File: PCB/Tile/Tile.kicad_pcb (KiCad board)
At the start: 2 copper layers, 100 x 86.6 mm, 41 parts, among them J1 Conn_01x05_Male, U1 HT16K33-28SOP

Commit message: [update] Tileの配線改善(DRC, 名前, ロゴ) #3
* DRCエラー(D17-Pad1)を修正
* 5-PINヘッダの名前をJ1からCN1に修正
* GardeningBoardのロゴの"Gardening"文字を右に移動
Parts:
- removed J1: Conn_01x05_Male, Connector_PinHeader_2.54mm:PinHeader_1x05_P2.54mm_Vertical
- added CN1: Conn_01x05_Male, Connector_PinHeader_2.54mm:PinHeader_1x05_P2.54mm_Vertical, F.Cu at (125.0, 92.5)
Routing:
- net Net-(D21-Pad2): track 61.7 -> 60.7 mm
- net GND: vias 47 -> 46

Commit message: (Tile) スレーブアドレス選択のシルク誤りを修正 #17
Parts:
- removed G***: LOGO, logos:logo_750dpi
- removed JP3: A0, Jumper:SolderJumper-2_P1.3mm_Open_RoundedPad1.0x1.5mm
- added A0: A0, Jumper:SolderJumper-2_P1.3mm_Open_RoundedPad1.0x1.5mm, B.Cu at (122.1, 79.3)
- renumbered JP2 to A1, JP1 to A2
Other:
- board text added: "@ext_sui 2020.09"
- board text added: "Tile Growing v1.1"
- board text removed: "@ext_sui 2020.05"
- board text removed: "Tile Growing v1.0"

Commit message: (Tile) ダイオードのシルクを D26 から D25 に修正 #17
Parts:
- renumbered D26 to D25
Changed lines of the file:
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@@
   (net 28 "Net-(D16-Pad2)")
   (net 29 "Net-(D17-Pad1)")
-  (net 30 "Net-(D26-Pad1)")
-  (net 31 +5V)
-  (net 32 "Net-(D9-Pad2)")
-  (net 33 "Net-(CN1-Pad4)")
+  (net 30 +5V)
+  (net 31 "Net-(D9-Pad2)")
+  (net 32 "Net-(CN1-Pad4)")
+  (net 33 "Net-(D25-Pad1)")
   (net_class Default "これはデフォルトのネット クラスです。"
     (clearance 0.2)
@@
     (add_net "Net-(D23-Pad2)")
     (add_net "Net-(D24-Pad2)")
-    (add_net "Net-(D26-Pad1)")
+    (add_net "Net-(D25-Pad1)")
     (add_net "Net-(D9-Pad2)")
     (add_net "Net-(JP1-Pad1)")
@@
       (net 4 "Net-(D10-Pad2)"))
     (pad 17 smd rect (at 4.7 -5.715 270) (size 2 0.6) (layers B.Cu B.Paste B.Mask)
-      (net 32 "Net-(D9-Pad2)"))
+      (net 31 "Net-(D9-Pad2)"))
     (pad 18 smd rect (at 4.7 -4.445 270) (size 2 0.6) (layers B.Cu B.Paste B.Mask)
       (net 27 "Net-(D24-Pad2)"))
@@
       (net 10 SDA))
     (pad 28 smd rect (at 4.7 8.255 270) (size 2 0.6) (layers B.Cu B.Paste B.Mask)
-      (net 31 +5V))
+      (net 30 +5V))
     (model ${KISYS3DMOD}/Package_SO.3dshapes/SOIC-28W_7.5x18.7mm_P1.27mm.wrl
       (at (xyz 0 0 0))
@@
     (fp_line (start 1.45 -0.7) (end -1.46 -0.7) (layer B.CrtYd) (width 0.05))
     (pad 1 smd rect (at -0.8 0 180) (size 0.8 0.8) (layers B.Cu B.Paste B.Mask)
-      (net 31 +5V))
+      (net 30 +5V))
     (pad 2 smd rect (at 0.8 0 180) (size 0.8 0.8) (layers B.Cu B.Paste B.Mask)
       (net 1 GND))
@@
     (tags "resistor 0603")
     (attr smd)
-    (fp_text reference D26 (at 3 0 180) (layer B.SilkS)
+    (fp_text reference D25 (at 3 0 180) (layer B.SilkS)
       (effects (font (size 1 1) (thickness 0.15)) (justify mirror))
     )
@@
     (fp_line (start -0.25 0) (end 0.25 -0.25) (layer B.SilkS) (width 0.15))
     (pad 1 smd rect (at -0.8 0 180) (size 0.8 0.8) (layers B.Cu B.Paste B.Mask)
-      (net 30 "Net-(D26-Pad1)"))
+      (net 33 "Net-(D25-Pad1)"))
     (pad 2 smd rect (at 0.8 0 180) (size 0.8 0.8) (layers B.Cu B.Paste B.Mask)
       (net 2 "Net-(D1-Pad1)"))
@@
     (fp_line (start -1.45 0.7) (end -1.45 -0.7) (layer B.SilkS) (width 0.12))
     (pad 2 smd rect (at 0.8 0 180) (size 0.8 0.8) (layers B.Cu B.Paste B.Mask)
-      (net 30 "Net-(D26-Pad1)"))
+      (net 33 "Net-(D25-Pad1)"))
     (pad 1 smd rect (at -0.8 0 180) (size 0.8 0.8) (layers B.Cu B.Paste B.Mask)
       (net 6 "Net-(JP1-Pad1)"))
@@
     (fp_line (start -1.45 0.7) (end -1.45 -0.7) (layer B.SilkS) (width 0.12))
     (pad 2 smd rect (at 0.8 0 180) (size 0.8 0.8) (layers B.Cu B.Paste B.Mask)
-      (net 30 "Net-(D26-Pad1)"))
+      (net 33 "Net-(D25-Pad1)"))
     (pad 1 smd rect (at -0.8 0 180) (size 0.8 0.8) (layers B.Cu B.Paste B.Mask)
       (net 7 "Net-(JP2-Pad1)"))
@@
       (net 8 "Net-(JP3-Pad1)"))
     (pad 2 smd rect (at 0.8 0 180) (size 0.8 0.8) (layers B.Cu B.Paste B.Mask)
-      (net 30 "Net-(D26-Pad1)"))
+      (net 33 "Net-(D25-Pad1)"))
     (model ${KISYS3DMOD}/Resistors_SMD.3dshapes/R_0603.wrl
       (at (xyz 0 0 0))
@@
     (fp_line (start -1.45 -0.7) (end -1.45 0.7) (layer F.SilkS) (width 0.12))
     (pad 2 smd rect (at 0.8 0 300) (size 0.8 0.8) (layers F.Cu F.Paste F.Mask)
-      (net 32 "Net-(D9-Pad2)"))
+      (net 31 "Net-(D9-Pad2)"))
     (pad 1 smd rect (at -0.8 0 300) (size 0.8 0.8) (layers F.Cu F.Paste F.Mask)
       (net 2 "Net-(D1-Pad1)"))
@@
     )
     (pad 1 thru_hole rect (at 0 0 90) (size 1.7 1.7) (drill 1) (layers *.Cu *.Mask)
-      (net 31 +5V))
+      (net 30 +5V))
     (pad 2 thru_hole oval (at 0 2.54 90) (size 1.7 1.7) (drill 1) (layers *.Cu *.Mask)
       (net 10 SDA))
@@
       (net 9 SCL))
     (pad 4 thru_hole oval (at 0 7.62 90) (size 1.7 1.7) (drill 1) (layers *.Cu *.Mask)
-      (net 33 "Net-(CN1-Pad4)"))
+      (net 32 "Net-(CN1-Pad4)"))
     (pad 5 thru_hole oval (at 0 10.16 90) (size 1.7 1.7) (drill 1) (layers *.Cu *.Mask)
       (net 1 GND))
@@
   (segment (start 129 139) (end 136 139) (width 0.25) (layer B.Cu) (net 29))
   (segment (start 136 139) (end 138 141) (width 0.25) (layer B.Cu) (net 29))
-  (segment (start 111.24713 81.753186) (end 111.24013 81.746186) (width 0.25) (layer B.Cu) (net 30))
-  (segment (start 115.03013 81.753186) (end 111.24713 81.753186) (width 0.25) (layer B.Cu) (net 30))
-  (segment (start 115.03013 80.253186) (end 115.03013 83.253186) (width 0.25) (layer B.Cu) (net 30))
-  (segment (start 128.695 86.75) (end 128.745 86.7) (width 0.5) (layer B.Cu) (net 31))
-  (segment (start 122.9 86.75) (end 128.695 86.75) (width 0.5) (layer B.Cu) (net 31))
-  (segment (start 128.745 88.755) (end 128.745 88.255) (width 0.5) (layer B.Cu) (net 31))
-  (segment (start 125 92.5) (end 128.745 88.755) (width 0.5) (layer B.Cu) (net 31))
-  (segment (start 128.745 88.255) (end 128.745 86.7) (width 0.5) (layer B.Cu) (net 31))
-  (segment (start 158.7 84.728718) (end 159.35 85.85) (width 0.25) (layer F.Cu) (net 32))
-  (via (at 159.35 85.85) (size 0.8) (drill 0.4) (layers F.Cu B.Cu) (net 32))
-  (segment (start 142.715 88.785) (end 142.715 86.7) (width 0.25) (layer B.Cu) (net 32))
-  (segment (start 143.93 90) (end 142.715 88.785) (width 0.25) (layer B.Cu) (net 32))
-  (segment (start 147.5 90) (end 143.93 90) (width 0.25) (layer B.Cu) (net 32))
-  (segment (start 152 85.85) (end 151.65 85.85) (width 0.25) (layer B.Cu) (net 32))
-  (segment (start 159.35 85.85) (end 152 85.85) (width 0.25) (layer B.Cu) (net 32))
-  (segment (start 147.5 90) (end 151.65 85.85) (width 0.25) (layer B.Cu) (net 32))
+  (segment (start 128.695 86.75) (end 128.745 86.7) (width 0.5) (layer B.Cu) (net 30))
+  (segment (start 122.9 86.75) (end 128.695 86.75) (width 0.5) (layer B.Cu) (net 30))
+  (segment (start 128.745 88.755) (end 128.745 88.255) (width 0.5) (layer B.Cu) (net 30))
+  (segment (start 125 92.5) (end 128.745 88.755) (width 0.5) (layer B.Cu) (net 30))
+  (segment (start 128.745 88.255) (end 128.745 86.7) (width 0.5) (layer B.Cu) (net 30))
+  (segment (start 158.7 84.728718) (end 159.35 85.85) (width 0.25) (layer F.Cu) (net 31))
+  (via (at 159.35 85.85) (size 0.8) (drill 0.4) (layers F.Cu B.Cu) (net 31))
+  (segment (start 142.715 88.785) (end 142.715 86.7) (width 0.25) (layer B.Cu) (net 31))
+  (segment (start 143.93 90) (end 142.715 88.785) (width 0.25) (layer B.Cu) (net 31))
+  (segment (start 147.5 90) (end 143.93 90) (width 0.25) (layer B.Cu) (net 31))
+  (segment (start 152 85.85) (end 151.65 85.85) (width 0.25) (layer B.Cu) (net 31))
+  (segment (start 159.35 85.85) (end 152 85.85) (width 0.25) (layer B.Cu) (net 31))
+  (segment (start 147.5 90) (end 151.65 85.85) (width 0.25) (layer B.Cu) (net 31))
+  (segment (start 111.24713 81.753186) (end 111.24013 81.746186) (width 0.25) (layer B.Cu) (net 33))
+  (segment (start 115.03013 81.753186) (end 111.24713 81.753186) (width 0.25) (layer B.Cu) (net 33))
+  (segment (start 115.03013 80.253186) (end 115.03013 83.253186) (width 0.25) (layer B.Cu) (net 33))
   (zone (net 1) (net_name GND) (layer B.Cu) (hatch edge 0.508)
     (connect_pads (clearance 0.508))

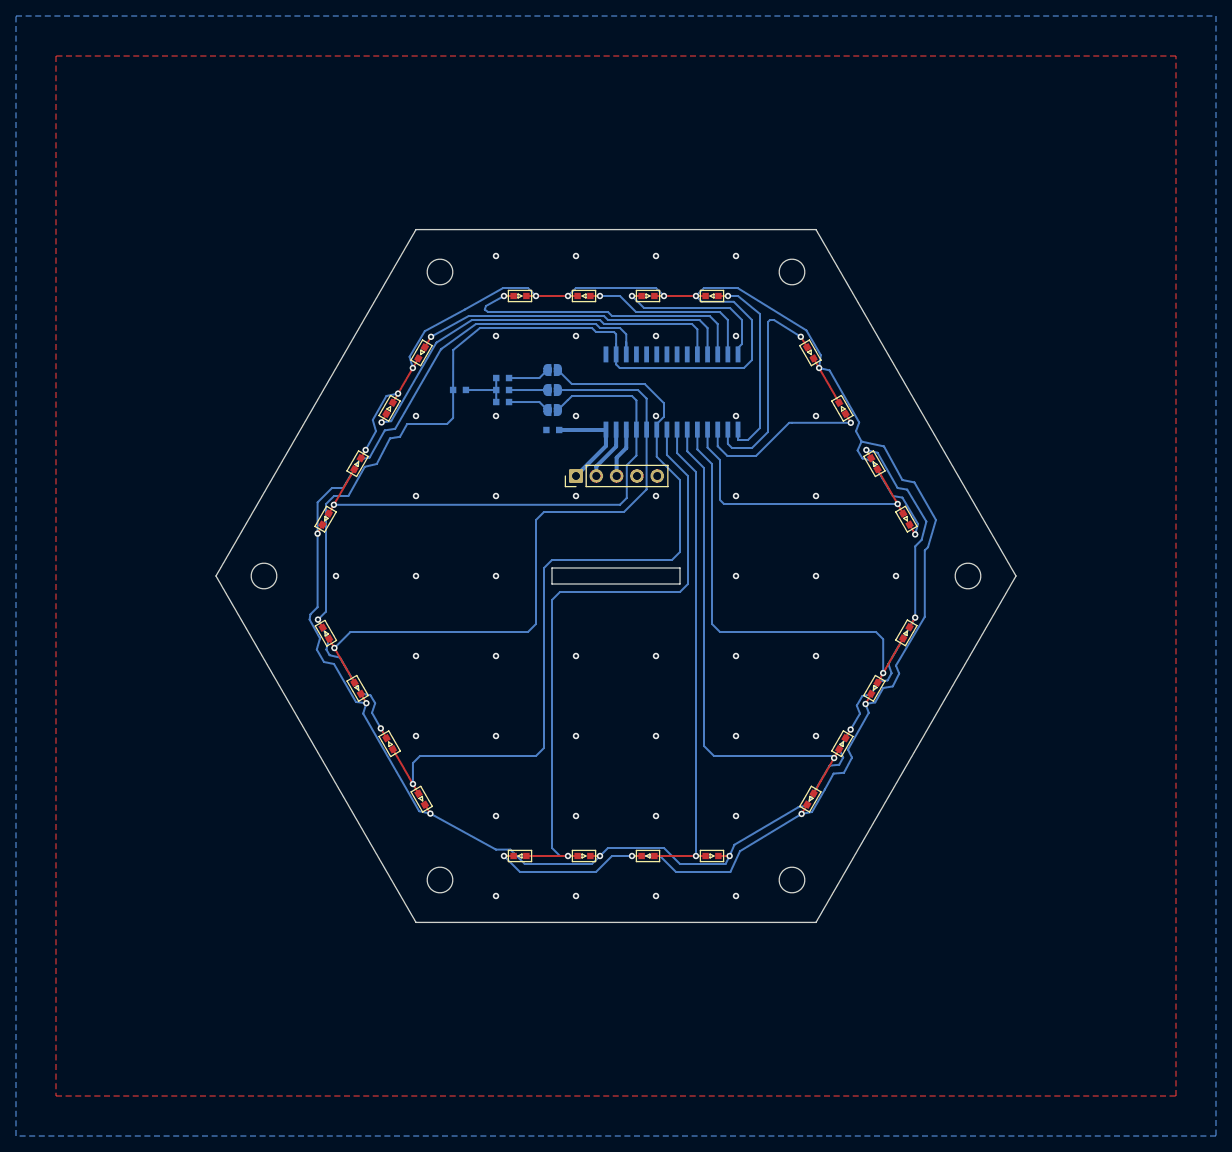
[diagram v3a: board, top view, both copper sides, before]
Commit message: (Tile) ベタ塗り無しで基板の色の変化を確認する試作版 #20
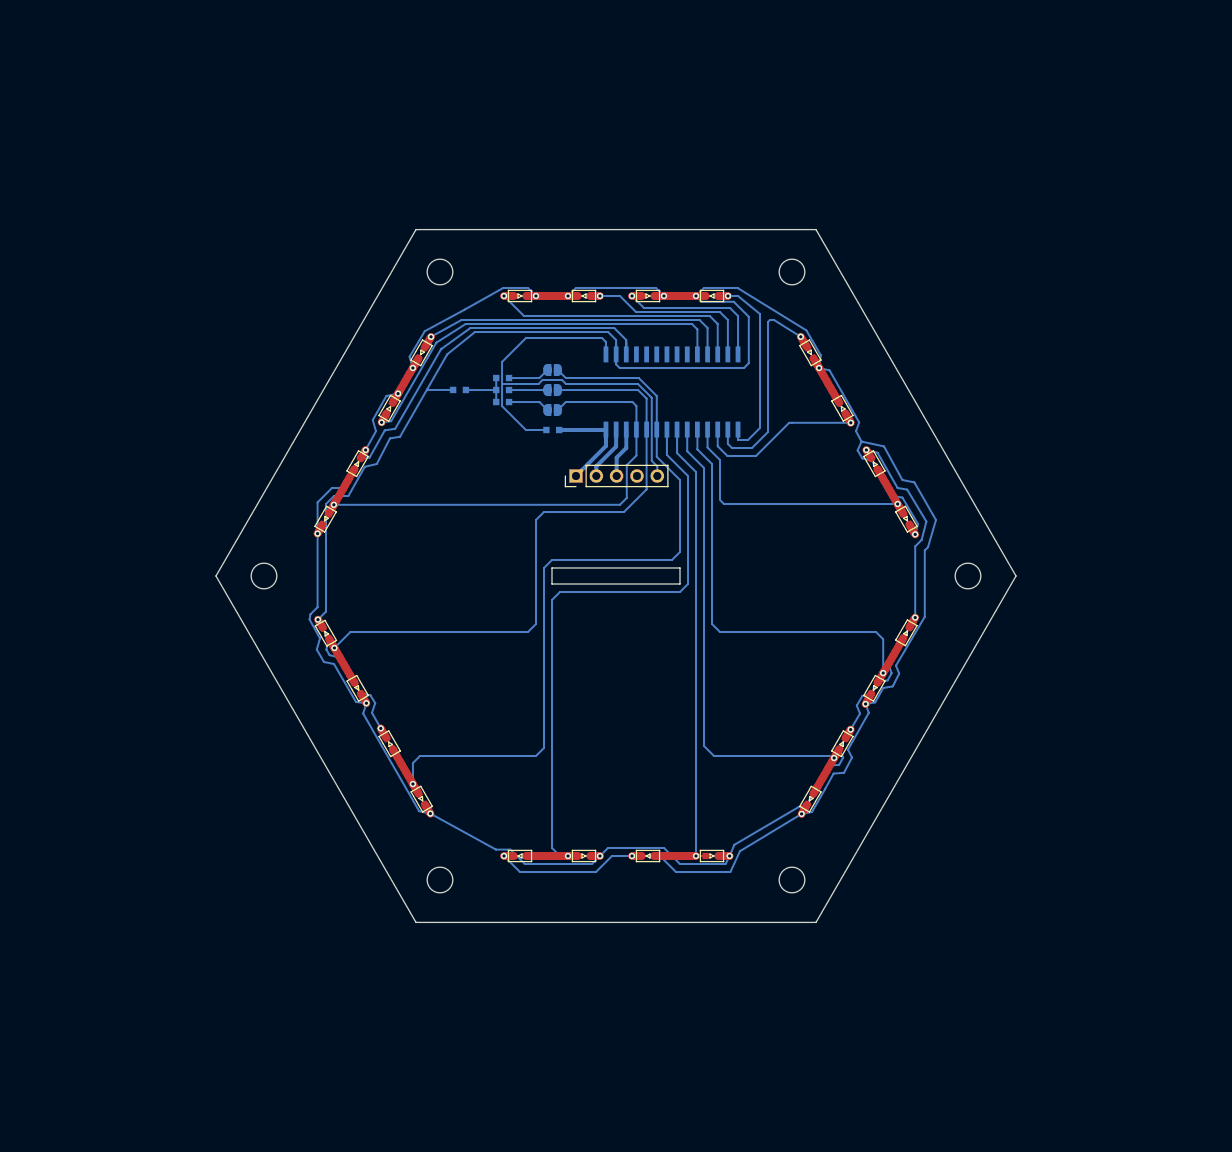
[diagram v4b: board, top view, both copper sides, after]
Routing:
- net GND: track 0.00 -> 58.2 mm, vias 46 -> 0
- net Net-(D14-Pad2): track 37.9 -> 33.2 mm
- net Net-(D1-Pad1): track 348.2 -> 346.7 mm
- net Net-(D1-Pad2): track 66.8 -> 65.8 mm
- net Net-(D17-Pad1): track 219.1 -> 218.3 mm
- net Net-(D19-Pad2): track 101.7 -> 100.9 mm
- removed copper zone on B.Cu, net GND
- removed copper zone on F.Cu, net GND
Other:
- board text added: "Tile Growing v1.1a"
- board text removed: "Tile Growing v1.1"
